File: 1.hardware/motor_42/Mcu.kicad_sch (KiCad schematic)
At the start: 0 parts

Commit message: 중간 저장
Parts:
- added U1: STM32F103CBTx, Package_QFP:LQFP-48_7x7mm_P0.5mm, symbol MCU_ST_STM32F1:STM32F103CBTx
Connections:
- new net: U1.23 (VSS), U1.35 (VSS), U1.47 (VSS)
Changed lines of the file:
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@@
 (kicad_sch
-	(version 20231120)
+	(version 20250114)
 	(generator "eeschema")
-	(generator_version "8.0")
+	(generator_version "9.0")
 	(paper "A4")
+	(symbol
+		(lib_id "MCU_ST_STM32F1:STM32F103CBTx")
+		(at 154.94 92.71 0)
+		(unit 1)
+		(exclude_from_sim no)
+		(in_bom yes)
+		(on_board yes)
+		(dnp no)
+		(fields_autoplaced yes)
+		(property "Reference" "U1"
+			(at 159.6233 133.35 0)
+			(effects
+				(font
+					(size 1.27 1.27)
+				)
+				(justify left)
+			)
+		)
+		(property "Value" "STM32F103CBTx"
+			(at 159.6233 135.89 0)
+			(effects
+				(font
+					(size 1.27 1.27)
+				)
+				(justify left)
+			)
+		)
+		(property "Footprint" "Package_QFP:LQFP-48_7x7mm_P0.5mm"
+			(at 139.7 130.81 0)
+			(effects
+				(font
+					(size 1.27 1.27)
+				)
+				(justify right)
+				(hide yes)
+			)
+		)
+		(property "Datasheet" "https://www.st.com/resource/en/datasheet/stm32f103cb.pdf"
+			(at 154.94 92.71 0)
+			(effects
+				(font
+					(size 1.27 1.27)
+				)
+				(hide yes)
+			)
+		)
+		(property "Description" "STMicroelectronics Arm Cortex-M3 MCU, 128KB flash, 20KB RAM, 72 MHz, 2.0-3.6V, 37 GPIO, LQFP48"
+			(at 154.94 92.71 0)
+			(effects
+				(font
+					(size 1.27 1.27)
+				)
+				(hide yes)
+			)
+		)
+		(pin "18"
+		)
+		(pin "43"
+		)
+		(pin "39"
+		)
+		(pin "24"
+		)
+		(pin "36"
+		)
+		(pin "47"
+		)
+		(pin "1"
+		)
+		(pin "46"
+		)
+		(pin "45"
+		)
+		(pin "27"
+		)
+		(pin "8"
+		)
+		(pin "28"
+		)
+		(pin "21"
+		)
+		(pin "26"
+		)
+		(pin "6"
+		)
+		(pin "3"
+		)
+		(pin "4"
+		)
+		(pin "2"
+		)
+		(pin "19"
+		)
+		(pin "40"
+		)
+		(pin "41"
+		)
+		(pin "5"
+		)
+		(pin "42"
+		)
+		(pin "44"
+		)
+		(pin "7"
+		)
+		(pin "20"
+		)
+		(pin "22"
+		)
+		(pin "25"
+		)
+		(pin "23"
+		)
+		(pin "35"
+		)
+		(pin "48"
+		)
+		(pin "13"
+		)
+		(pin "32"
+		)
+		(pin "31"
+		)
+		(pin "29"
+		)
+		(pin "14"
+		)
+		(pin "17"
+		)
+		(pin "34"
+		)
+		(pin "16"
+		)
+		(pin "38"
+		)
+		(pin "15"
+		)
+		(pin "11"
+		)
+		(pin "30"
+		)
+		(pin "10"
+		)
+		(pin "12"
+		)
+		(pin "33"
+		)
+		(pin "37"
+		)
+		(pin "9"
+		)
+		(instances
+			(project ""
+				(path "/3c5de6a8-6840-43a5-a2fb-24dbb7f0450d/91ecfca5-1fde-4bfb-b396-1bb710e5b1bd"
+					(reference "U1")
+					(unit 1)
+				)
+			)
+		)
+	)
 )

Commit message: 중간 저장
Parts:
- added C10: 4.7uF/16V, symbol Device:C_Small_US
- added C11, C12, C13, C14: 0.1uF/50V, symbol Device:C_Small_US
- added C21, C22: 12pF/50V, symbol Device:C_Small_US
- added R10, R9: 10k/0.063w, symbol Device:R_Small_US
- added Y1: YSX321SL_12Mhz, symbol Device:Crystal_GND24_Small
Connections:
- net 3V3: now reaches U1.1 (VBAT)
- net 3V3: now also U1.24 (VDD), U1.36 (VDD), U1.48 (VDD), U1.9 (VDDA), C10.1, C11.1, C12.1, C13.1, R10.2
- net GND: now reaches U1.23 (VSS), U1.35 (VSS), U1.47 (VSS)
- net GND: now also U1.8 (VSSA), C10.2, C11.2, C12.2, C13.2, C14.2, C21.2, C22.2, R9.2, Y1.2, Y1.4
- net at U1.44 (BOOT0): now also R9.1
- net 12Mhz_IN: now reaches U1.5 (PD0)
- net 12Mhz_IN: now also C21.1, Y1.1
- net 12Mhz_OUT: now reaches U1.6 (PD1)
- net 12Mhz_OUT: now also C22.1, Y1.3
- net at U1.7 (NRST): now also C14.1, R10.1

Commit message: 중간 저장
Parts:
- added C23: 0.1uF/50V, symbol Device:C_Small_US
- added R12: 10k/0.063w, symbol Device:R_Small_US
- added RT1: NCP18XH103F03RB, THRMC1608X95N, symbol SamacSys_Parts:NCP18XH103F03RB
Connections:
- net 3V3: now also RT1.2
- net GND: now also C23.2, R12.1
- new net TEMP: C23.1, R12.2, RT1.1
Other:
- moved on the sheet: C10, C11, C12, C13, C14, C21, C22, R10, R9, U1, Y1

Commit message: 중간 저장
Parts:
- renumbered C10 to C14, C11 to C15, C12 to C16, C13 to C17, C21 to C18, C22 to C19, C14 to C20, C23 to C21, R9 to R10, R12 to R11, R10 to R9, U1 to U2
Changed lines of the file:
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@@
+		)
+	)
+	(global_label "SPI2_NSS"
+		(shape passive)
+		(at 212.09 91.44 0)
+		(fields_autoplaced yes)
+		(effects
+			(font
+				(size 1.27 1.27)
+			)
+			(justify left)
+		)
+		(property "Intersheetrefs" "${INTERSHEET_REFS}"
+			(at 222.9748 91.44 0)
+			(effects
+				(font
+					(size 1.27 1.27)
+				)
+				(justify left)
+				(hide yes)
+			)
 		)
 	)
@@
 		)
 	)
+	(global_label "SPI2_SCK"
+		(shape passive)
+		(at 212.09 93.98 0)
+		(fields_autoplaced yes)
+		(effects
+			(font
+				(size 1.27 1.27)
+			)
+			(justify left)
+		)
+		(property "Intersheetrefs" "${INTERSHEET_REFS}"
+			(at 222.9748 93.98 0)
+			(effects
+				(font
+					(size 1.27 1.27)
+				)
+				(justify left)
+				(hide yes)
+			)
+		)
+	)
 	(global_label "SPI1_MISO"
 		(shape passive)
@@
 		)
 	)
+	(global_label "SPI2_MISO"
+		(shape passive)
+		(at 212.09 96.52 0)
+		(fields_autoplaced yes)
+		(effects
+			(font
+				(size 1.27 1.27)
+			)
+			(justify left)
+		)
+		(property "Intersheetrefs" "${INTERSHEET_REFS}"
+			(at 223.8215 96.52 0)
+			(effects
+				(font
+					(size 1.27 1.27)
+				)
+				(justify left)
+				(hide yes)
+			)
+		)
+	)
 	(global_label "3V3_MCU"
 		(shape passive)
@@
 		(property "Intersheetrefs" "${INTERSHEET_REFS}"
 			(at 156.0276 29.21 0)
+			(effects
+				(font
+					(size 1.27 1.27)
+				)
+				(justify left)
+				(hide yes)
+			)
+		)
+	)
+	(global_label "SPI2_MOSI"
+		(shape passive)
+		(at 212.09 99.06 0)
+		(fields_autoplaced yes)
+		(effects
+			(font
+				(size 1.27 1.27)
+			)
+			(justify left)
+		)
+		(property "Intersheetrefs" "${INTERSHEET_REFS}"
+			(at 223.8215 99.06 0)
 			(effects
 				(font
@@
 		(on_board yes)
 		(dnp no)
-		(property "Reference" "C14"
+		(property "Reference" "C20"
 			(at 118.11 64.8969 0)
 			(effects
@@
 			(project "motor_42"
 				(path "/3c5de6a8-6840-43a5-a2fb-24dbb7f0450d/91ecfca5-1fde-4bfb-b396-1bb710e5b1bd"
-					(reference "C14")
+					(reference "C20")
 					(unit 1)
 				)
@@
 		(on_board yes)
 		(dnp no)
-		(property "Reference" "C22"
+		(property "Reference" "C19"
 			(at 134.366 30.226 0)
 			(effects
@@
 			(project "motor_42"
 				(path "/3c5de6a8-6840-43a5-a2fb-24dbb7f0450d/91ecfca5-1fde-4bfb-b396-1bb710e5b1bd"
-					(reference "C22")
+					(reference "C19")
 					(unit 1)
 				)
@@
 		(dnp no)
 		(fields_autoplaced yes)
-		(property "Reference" "#PWR013"
+		(property "Reference" "#PWR025"
 			(at 154.94 147.32 0)
 			(effects
@@
 			(project "motor_42"
 				(path "/3c5de6a8-6840-43a5-a2fb-24dbb7f0450d/91ecfca5-1fde-4bfb-b396-1bb710e5b1bd"
-					(reference "#PWR013")
+					(reference "#PWR025")
 					(unit 1)
 				)
@@
 		(dnp no)
 		(fields_autoplaced yes)
-		(property "Reference" "#PWR019"
+		(property "Reference" "#PWR023"
 			(at 121.92 85.09 0)
 			(effects
@@
 			(project "motor_42"
 				(path "/3c5de6a8-6840-43a5-a2fb-24dbb7f0450d/91ecfca5-1fde-4bfb-b396-1bb710e5b1bd"
-					(reference "#PWR019")
+					(reference "#PWR023")
 					(unit 1)
 				)
@@
 		(on_board yes)
 		(dnp no)
-		(property "Reference" "R9"
+		(property "Reference" "R10"
 			(at 120.65 70.866 0)
 			(effects
@@
 			(project "motor_42"
 				(path "/3c5de6a8-6840-43a5-a2fb-24dbb7f0450d/91ecfca5-1fde-4bfb-b396-1bb710e5b1bd"
-					(reference "R9")
+					(reference "R10")
 					(unit 1)
 				)
@@
 		(on_board yes)
 		(dnp no)
-		(property "Reference" "C21"
+		(property "Reference" "C18"
 			(at 125.222 30.226 0)
 			(effects
@@
 			(project "motor_42"
 				(path "/3c5de6a8-6840-43a5-a2fb-24dbb7f0450d/91ecfca5-1fde-4bfb-b396-1bb710e5b1bd"
-					(reference "C21")
+					(reference "C18")
 					(unit 1)
 				)
@@
 		(on_board yes)
 		(dnp no)
-		(property "Reference" "C12"
+		(property "Reference" "C16"
 			(at 73.66 28.0669 0)
 			(effects
@@
 			(project "motor_42"
 				(path "/3c5de6a8-6840-43a5-a2fb-24dbb7f0450d/91ecfca5-1fde-4bfb-b396-1bb710e5b1bd"
-					(reference "C12")
+					(reference "C16")
 					(unit 1)
 				)
@@
 		(on_board yes)
 		(dnp no)
-		(property "Reference" "#PWR029"
+		(property "Reference" "#PWR021"
 			(at 132.08 46.99 0)
 			(effects
@@
 			(project "motor_42"
 				(path "/3c5de6a8-6840-43a5-a2fb-24dbb7f0450d/91ecfca5-1fde-4bfb-b396-1bb710e5b1bd"
-					(reference "#PWR029")
+					(reference "#PWR021")
 					(unit 1)
 				)
@@
 		(dnp no)
 		(fields_autoplaced yes)
-		(property "Reference" "#PWR018"
+		(property "Reference" "#PWR020"
 			(at 82.55 40.64 0)
 			(effects
@@
 			(project "motor_42"
 				(path "/3c5de6a8-6840-43a5-a2fb-24dbb7f0450d/91ecfca5-1fde-4bfb-b396-1bb710e5b1bd"
-					(reference "#PWR018")
+					(reference "#PWR020")
 					(unit 1)
 				)
@@
 		(on_board yes)
 		(dnp no)
-		(property "Reference" "R12"
+		(property "Reference" "R11"
 			(at 48.768 79.248 0)
 			(effects
@@
 			(project "motor_42"
 				(path "/3c5de6a8-6840-43a5-a2fb-24dbb7f0450d/91ecfca5-1fde-4bfb-b396-1bb710e5b1bd"
-					(reference "R12")
+					(reference "R11")
 					(unit 1)
 				)
@@
 		(on_board yes)
 		(dnp no)
-		(property "Reference" "R10"
+		(property "Reference" "R9"
 			(at 113.538 55.118 0)
 			(effects
@@
 			(project "motor_42"
 				(path "/3c5de6a8-6840-43a5-a2fb-24dbb7f0450d/91ecfca5-1fde-4bfb-b396-1bb710e5b1bd"
-					(reference "R10")
+					(reference "R9")
 					(unit 1)
 				)
@@
 		(on_board yes)
 		(dnp no)
-		(property "Reference" "#PWR020"
+		(property "Reference" "#PWR022"
 			(at 115.57 77.47 0)
 			(effects
@@
 			(project "motor_42"
 				(path "/3c5de6a8-6840-43a5-a2fb-24dbb7f0450d/91ecfca5-1fde-4bfb-b396-1bb710e5b1bd"
-					(reference "#PWR020")
+					(reference "#PWR022")
 					(unit 1)
 				)
@@
 		(on_board yes)
 		(dnp no)
-		(property "Reference" "#PWR030"
+		(property "Reference" "#PWR024"
 			(at 50.8 96.52 0)
 			(effects
@@
 			(project "motor_42"
 				(path "/3c5de6a8-6840-43a5-a2fb-24dbb7f0450d/91ecfca5-1fde-4bfb-b396-1bb710e5b1bd"
-					(reference "#PWR030")
+					(reference "#PWR024")
 					(unit 1)
 				)
@@
 		(dnp no)
 		(fields_autoplaced yes)
-		(property "Reference" "#PWR015"
+		(property "Reference" "#PWR017"
 			(at 48.26 40.64 0)
 			(effects
@@
 			(project "motor_42"
 				(path "/3c5de6a8-6840-43a5-a2fb-24dbb7f0450d/91ecfca5-1fde-4bfb-b396-1bb710e5b1bd"
-					(reference "#PWR015")
+					(reference "#PWR017")
 					(unit 1)
 				)
@@
 		(dnp no)
 		(fields_autoplaced yes)
-		(property "Reference" "U1"
+		(property "Reference" "U2"
 			(at 159.6233 137.16 0)
 			(effects
@@
 			(project ""
 				(path "/3c5de6a8-6840-43a5-a2fb-24dbb7f0450d/91ecfca5-1fde-4bfb-b396-1bb710e5b1bd"
-					(reference "U1")
+					(reference "U2")
 					(unit 1)
 				)
@@
 		(on_board yes)
 		(dnp no)
-		(property "Reference" "C10"
+		(property "Reference" "C14"
 			(at 50.8 28.0669 0)
 			(effects
@@
 			(project "motor_42"
 				(path "/3c5de6a8-6840-43a5-a2fb-24dbb7f0450d/91ecfca5-1fde-4bfb-b396-1bb710e5b1bd"
-					(reference "C10")
+					(reference "C14")
 					(unit 1)
 				)
@@
 		(on_board yes)
 		(dnp no)
-		(property "Reference" "C11"
+		(property "Reference" "C15"
 			(at 62.23 28.0669 0)
 			(effects
@@
 			(project "motor_42"
 				(path "/3c5de6a8-6840-43a5-a2fb-24dbb7f0450d/91ecfca5-1fde-4bfb-b396-1bb710e5b1bd"
-					(reference "C11")
+					(reference "C15")
 					(unit 1)
 				)
@@
 		(on_board yes)
 		(dnp no)
-		(property "Reference" "C23"
+		(property "Reference" "C21"
 			(at 41.91 80.1369 0)
 			(effects
@@
 			(project "motor_42"
 				(path "/3c5de6a8-6840-43a5-a2fb-24dbb7f0450d/91ecfca5-1fde-4bfb-b396-1bb710e5b1bd"
-					(reference "C23")
+					(reference "C21")
 					(unit 1)
 				)
@@
 		(on_board yes)
 		(dnp no)
-		(property "Reference" "C13"
+		(property "Reference" "C17"
 			(at 85.09 28.0669 0)
 			(effects
@@
 			(project "motor_42"
 				(path "/3c5de6a8-6840-43a5-a2fb-24dbb7f0450d/91ecfca5-1fde-4bfb-b396-1bb710e5b1bd"
-					(reference "C13")
+					(reference "C17")
 					(unit 1)
 				)
@@
 		(dnp no)
 		(fields_autoplaced yes)
-		(property "Reference" "#PWR016"
+		(property "Reference" "#PWR018"
 			(at 59.69 40.64 0)
 			(effects
@@
 			(project "motor_42"
 				(path "/3c5de6a8-6840-43a5-a2fb-24dbb7f0450d/91ecfca5-1fde-4bfb-b396-1bb710e5b1bd"
-					(reference "#PWR016")
+					(reference "#PWR018")
 					(unit 1)
 				)
@@
 		(dnp no)
 		(fields_autoplaced yes)
-		(property "Reference" "#PWR017"
+		(property "Reference" "#PWR019"
 			(at 71.12 40.64 0)
 			(effects
@@
 			(project "motor_42"
 				(path "/3c5de6a8-6840-43a5-a2fb-24dbb7f0450d/91ecfca5-1fde-4bfb-b396-1bb710e5b1bd"
-					(reference "#PWR017")
+					(reference "#PWR019")
 					(unit 1)
 				)

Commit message: 회로도 대충 완성
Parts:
- added C15, C19: 0.1uF/16V, Capacitor_SMD:C_0402_1005Metric, symbol Device:C_Small_US
- added LED1: LED_0603_Red_WIFI, PCM_LED_SMD_AKL:LED_0603_1608Metric, symbol PCM_LED_AKL:LED_0603_Red
- added LED2: LED_0603_Blue_BLE, PCM_LED_SMD_AKL:LED_0603_1608Metric, symbol PCM_LED_AKL:LED_0603_Blue
- added R11, R13: 10K/0.063w, Resistor_SMD:R_0402_1005Metric, symbol Device:R_Small_US
- added R12, R37, R38, R9: 4.7K/0.063w, Resistor_SMD:R_0402_1005Metric, symbol Device:R_Small_US
- added R16, R17: 0R/0.063w, Resistor_SMD:R_0402_1005Metric, symbol Device:R_Small_US
- added S1, S2: TSB008A2518A, SamacSys_Parts:TSB008A2518A, symbol SamacSys_Parts:TSB008A2518A
- R10: renamed from R11; footprint (none) -> Resistor_SMD:R_0402_1005Metric
- R14: renamed from R9; footprint (none) -> Resistor_SMD:R_0402_1005Metric
- R15: renamed from R10; footprint (none) -> Resistor_SMD:R_0402_1005Metric
- RT1: footprint THRMC1608X95N -> SamacSys_Parts:THRMC1608X95N
- renumbered C21 to C14, C14 to C16, C15 to C17, C16 to C18, C17 to C20, C20 to C21, C18 to C22, C19 to C23
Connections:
- net 3V3: now also R11.1, R12.1, R13.1, R37.1, R38.1, R9.1
- net ADC_ENC: now also U2.14 (PA4)
- net ADC_VREF_2V5: now also U2.10 (PA0)
- net BTN1: now also U2.40 (PB4), C15.1, R11.2, S1.1 (COM)
- net BTN2: now also U2.41 (PB5), C19.1, R13.2, S2.1 (COM)
- net CAN_RX: now also U2.45 (PB8)
- net CAN_TX: now also U2.46 (PB9)
- net GND: now also C15.2, C19.2, S1.2 (NO), S2.2 (NO)
- net MT6816_CSN: now also U2.18 (PB0)
- net SPI1_CLK: now also U2.15 (PA5)
- net SPI1_MISO: now also U2.16 (PA6)
- net SPI1_MOSI: now also U2.17 (PA7)
- net SWCLK: now also U2.37 (PA14)
- net SWDIO: now also U2.34 (PA13)
- net TEMP: now also U2.11 (PA1)
- net UART1_RX: now also U2.43 (PB7)
- net UART1_TX: now also U2.42 (PB6)
- net ESP32_UART_RX: now reaches U2.12 (PA2)
- net ESP32_UART_RX: now also R37.2
- net ESP32_UART_TX: now reaches U2.13 (PA3)
- net ESP32_UART_TX: now also R38.2
- net WS2812_SIGNAL: now reaches U2.21 (PB10)
- net IN_B-: now reaches U2.25 (PB12)
- net IN_B+: now reaches U2.26 (PB13)
- net IN_A-: now reaches U2.27 (PB14)
- net IN_A+: now reaches U2.28 (PB15)
- net VREF_PWM_A: now reaches U2.29 (PA8)
- net VREF_PWM_B: now reaches U2.30 (PA9)
- net at U2.32 (PA11): now also R16.2
- net at U2.33 (PA12): now also R17.2
- net LED1: now reaches U2.38 (PA15)
- net LED1: now also LED1.1 (K)
- net LED2: now reaches U2.39 (PB3)
- net LED2: now also LED2.1 (K)
- new net: LED1.2 (A), R9.2
- new net: LED2.2 (A), R12.2
- new net USB_DM: R16.1
- new net USB_DP: R17.1
- no-connect marks 0 -> 7

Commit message: 수정
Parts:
- C14, C17, C18, C20, C21, C22, C23: footprint (none) -> Capacitor_SMD:C_0402_1005Metric
- C16: value 4.7uF/16V -> 4.7uF/10V; footprint (none) -> Capacitor_SMD:C_0603_1608Metric
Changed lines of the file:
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@@
 			)
 		)
-		(property "Footprint" ""
+		(property "Footprint" "Capacitor_SMD:C_0402_1005Metric"
 			(at 115.57 66.04 0)
 			(effects
@@
 			)
 		)
-		(property "Footprint" ""
+		(property "Footprint" "Capacitor_SMD:C_0402_1005Metric"
 			(at 138.43 31.75 0)
 			(effects
@@
 			)
 		)
-		(property "Footprint" ""
+		(property "Footprint" "Capacitor_SMD:C_0402_1005Metric"
 			(at 124.46 31.75 0)
 			(effects
@@
 			)
 		)
-		(property "Footprint" ""
+		(property "Footprint" "Capacitor_SMD:C_0402_1005Metric"
 			(at 71.12 29.21 0)
 			(effects
@@
 			)
 		)
-		(property "Value" "4.7uF/16V"
+		(property "Value" "4.7uF/10V"
 			(at 48.768 31.242 0)
 			(effects
@@
 			)
 		)
-		(property "Footprint" ""
+		(property "Footprint" "Capacitor_SMD:C_0603_1608Metric"
 			(at 48.26 29.21 0)
 			(effects
@@
 			)
 		)
-		(property "Footprint" ""
+		(property "Footprint" "Capacitor_SMD:C_0402_1005Metric"
 			(at 59.69 29.21 0)
 			(effects
@@
 			)
 		)
-		(property "Footprint" ""
+		(property "Footprint" "Capacitor_SMD:C_0402_1005Metric"
 			(at 39.37 81.28 0)
 			(effects
@@
 			)
 		)
-		(property "Footprint" ""
+		(property "Footprint" "Capacitor_SMD:C_0402_1005Metric"
 			(at 82.55 29.21 0)
 			(effects

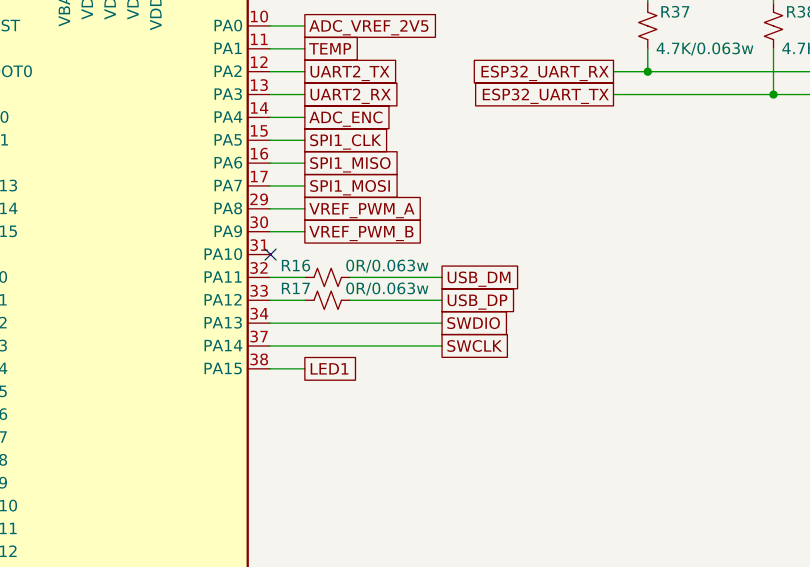
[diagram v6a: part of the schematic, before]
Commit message: 3V3 LDO변경 및 대략적 위치 세팅
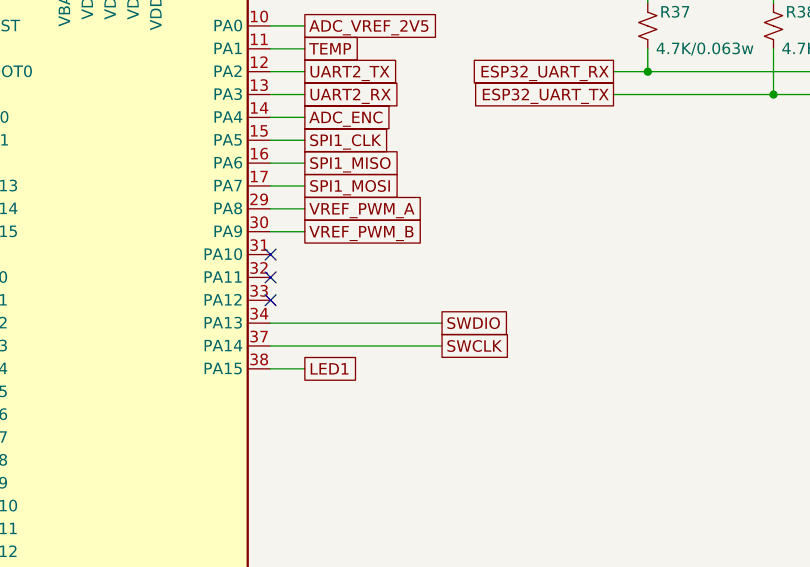
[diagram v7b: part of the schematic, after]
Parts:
- removed R16, R17: 0R/0.063w, Resistor_SMD:R_0402_1005Metric, symbol Device:R_Small_US
- Y1: footprint (none) -> Crystal:Crystal_SMD_3225-4Pin_3.2x2.5mm
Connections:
- no-connect marks 7 -> 9
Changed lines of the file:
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@@
 		(at 137.16 81.28)
 	)
+	(no_connect
+		(at 172.72 93.98)
+	)
+	(no_connect
+		(at 172.72 91.44)
+	)
 	(wire
 		(pts
@@
 	(wire
 		(pts
-			(xy 172.72 93.98) (xy 176.53 93.98)
-		)
-		(stroke
-			(width 0)
-			(type default)
-		)
-	)
-	(wire
-		(pts
 			(xy 228.6 60.96) (xy 228.6 57.15)
 		)
@@
 	(wire
 		(pts
-			(xy 181.61 93.98) (xy 191.77 93.98)
-		)
-		(stroke
-			(width 0)
-			(type default)
-		)
-	)
-	(wire
-		(pts
 			(xy 133.35 127) (xy 137.16 127)
 		)
@@
 	(wire
 		(pts
-			(xy 181.61 91.44) (xy 191.77 91.44)
-		)
-		(stroke
-			(width 0)
-			(type default)
-		)
-	)
-	(wire
-		(pts
 			(xy 35.56 134.62) (xy 41.91 134.62)
 		)
@@
 	(wire
 		(pts
-			(xy 172.72 91.44) (xy 176.53 91.44)
-		)
-		(stroke
-			(width 0)
-			(type default)
-		)
-	)
-	(wire
-		(pts
 			(xy 50.8 73.66) (xy 50.8 76.2)
 		)
@@
 		)
 	)
-	(global_label "USB_DM"
-		(shape passive)
-		(at 191.77 91.44 0)
-		(fields_autoplaced yes)
-		(effects
-			(font
-				(size 1.27 1.27)
-			)
-			(justify left)
-		)
-		(property "Intersheetrefs" "${INTERSHEET_REFS}"
-			(at 201.1429 91.44 0)
-			(effects
-				(font
-					(size 1.27 1.27)
-				)
-				(justify left)
-				(hide yes)
-			)
-		)
-	)
 	(global_label "IN_B-"
 		(shape passive)
@@
 		)
 	)
-	(global_label "USB_DP"
-		(shape passive)
-		(at 191.77 93.98 0)
-		(fields_autoplaced yes)
-		(effects
-			(font
-				(size 1.27 1.27)
-			)
-			(justify left)
-		)
-		(property "Intersheetrefs" "${INTERSHEET_REFS}"
-			(at 200.9615 93.98 0)
-			(effects
-				(font
-					(size 1.27 1.27)
-				)
-				(justify left)
-				(hide yes)
-			)
-		)
-	)
 	(global_label "UART2_RX"
 		(shape passive)
@@
 	(symbol
 		(lib_id "Device:R_Small_US")
-		(at 179.07 93.98 270)
-		(unit 1)
-		(exclude_from_sim no)
-		(in_bom yes)
-		(on_board yes)
-		(dnp no)
-		(property "Reference" "R17"
-			(at 175.514 92.71 90)
-			(effects
-				(font
-					(size 1.27 1.27)
-				)
-			)
-		)
-		(property "Value" "0R/0.063w"
-			(at 185.674 92.71 90)
-			(effects
-				(font
-					(size 1.27 1.27)
-				)
-			)
-		)
-		(property "Footprint" "Resistor_SMD:R_0402_1005Metric"
-			(at 179.07 93.98 0)
-			(effects
-				(font
-					(size 1.27 1.27)
-				)
-				(hide yes)
-			)
-		)
-		(property "Datasheet" "~"
-			(at 179.07 93.98 0)
-			(effects
-				(font
-					(size 1.27 1.27)
-				)
-				(hide yes)
-			)
-		)
-		(property "Description" "Resistor, small US symbol"
-			(at 179.07 93.98 0)
-			(effects
-				(font
-					(size 1.27 1.27)
-				)
-				(hide yes)
-			)
-		)
-		(pin "2"
-		)
-		(pin "1"
-		)
-		(instances
-			(project "motor_42"
-				(path "/3c5de6a8-6840-43a5-a2fb-24dbb7f0450d/91ecfca5-1fde-4bfb-b396-1bb710e5b1bd"
-					(reference "R17")
-					(unit 1)
-				)
-			)
-		)
-	)
-	(symbol
-		(lib_id "Device:R_Small_US")
 		(at 95.25 138.43 0)
 		(unit 1)
@@
 			)
 		)
-		(property "Footprint" ""
+		(property "Footprint" "Crystal:Crystal_SMD_3225-4Pin_3.2x2.5mm"
 			(at 132.08 29.21 0)
 			(effects
@@
 					(unit 1)
 				)
-			)
-		)
-	)
-	(symbol
-		(lib_id "Device:R_Small_US")
-		(at 179.07 91.44 270)
-		(unit 1)
-		(exclude_from_sim no)
-		(in_bom yes)
-		(on_board yes)
-		(dnp no)
-		(property "Reference" "R16"
-			(at 175.514 90.17 90)
-			(effects
-				(font
-					(size 1.27 1.27)
-				)
-			)
-		)
-		(property "Value" "0R/0.063w"
-			(at 185.674 90.17 90)
-			(effects
-				(font
-					(size 1.27 1.27)
-				)
-			)
-		)
-		(property "Footprint" "Resistor_SMD:R_0402_1005Metric"
-			(at 179.07 91.44 0)
-			(effects
-				(font
-					(size 1.27 1.27)
-				)
-				(hide yes)
-			)
-		)
-		(property "Datasheet" "~"
-			(at 179.07 91.44 0)
-			(effects
-				(font
-					(size 1.27 1.27)
-				)
-				(hide yes)
-			)
-		)
-		(property "Description" "Resistor, small US symbol"
-			(at 179.07 91.44 0)
-			(effects
-				(font
-					(size 1.27 1.27)
-				)
-				(hide yes)
-			)
-		)
-		(pin "2"
-		)
-		(pin "1"
-		)
-		(instances
-			(project "motor_42"
-				(path "/3c5de6a8-6840-43a5-a2fb-24dbb7f0450d/91ecfca5-1fde-4bfb-b396-1bb710e5b1bd"
-					(reference "R16")
-					(unit 1)
-				)

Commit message: 중간 저장
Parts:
- removed R37, R38: 4.7K/0.063w, Resistor_SMD:R_0402_1005Metric, symbol Device:R_Small_US
- added C35: 0.1uF/50V, Capacitor_SMD:C_0402_1005Metric, symbol Device:C_Small_US
- added C36: 1uF/10V, Capacitor_SMD:C_0402_1005Metric, symbol Device:C_Small_US
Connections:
- net 3V3: now also C35.1, C36.1
- net GND: now also C35.2, C36.2
